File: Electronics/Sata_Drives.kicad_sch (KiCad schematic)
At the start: 66 parts, among them J20 47018-2000, J21 47018-2000, Q2 NPN, Q3 PMOS, Q4 NPN, Q5 PMOS, Q6 PMOS, Q7 NPN, Q8 NPN, Q9 PMOS, U10 JMS561, U9 W25X40CLSN, Y1 30MHz

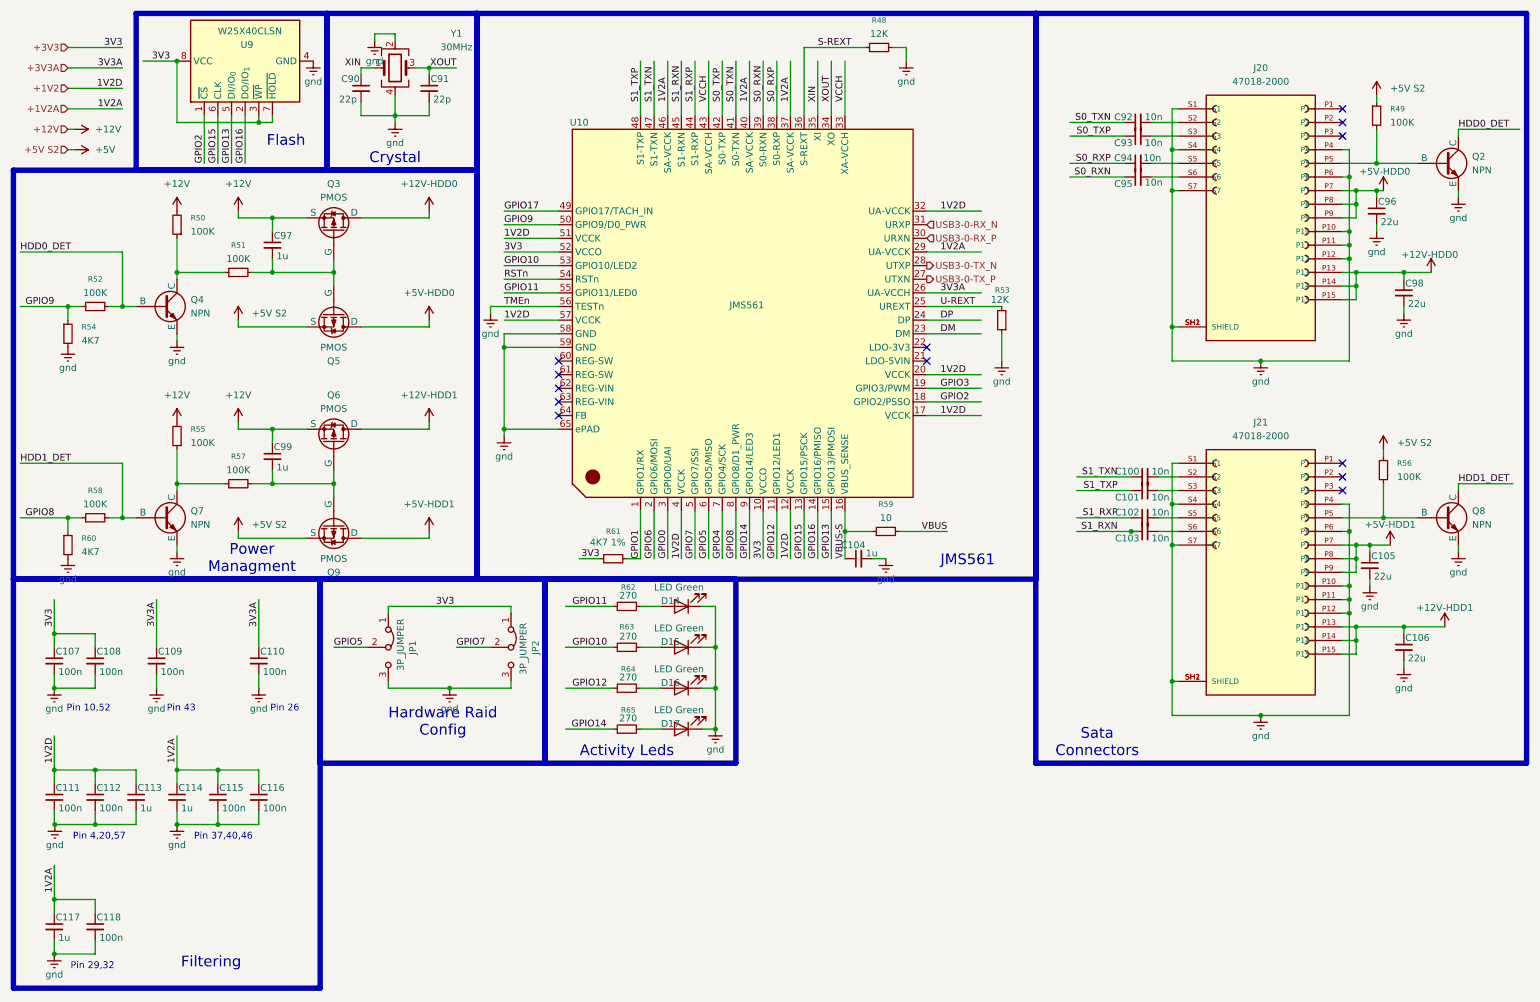
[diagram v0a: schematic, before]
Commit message: Changed sata port
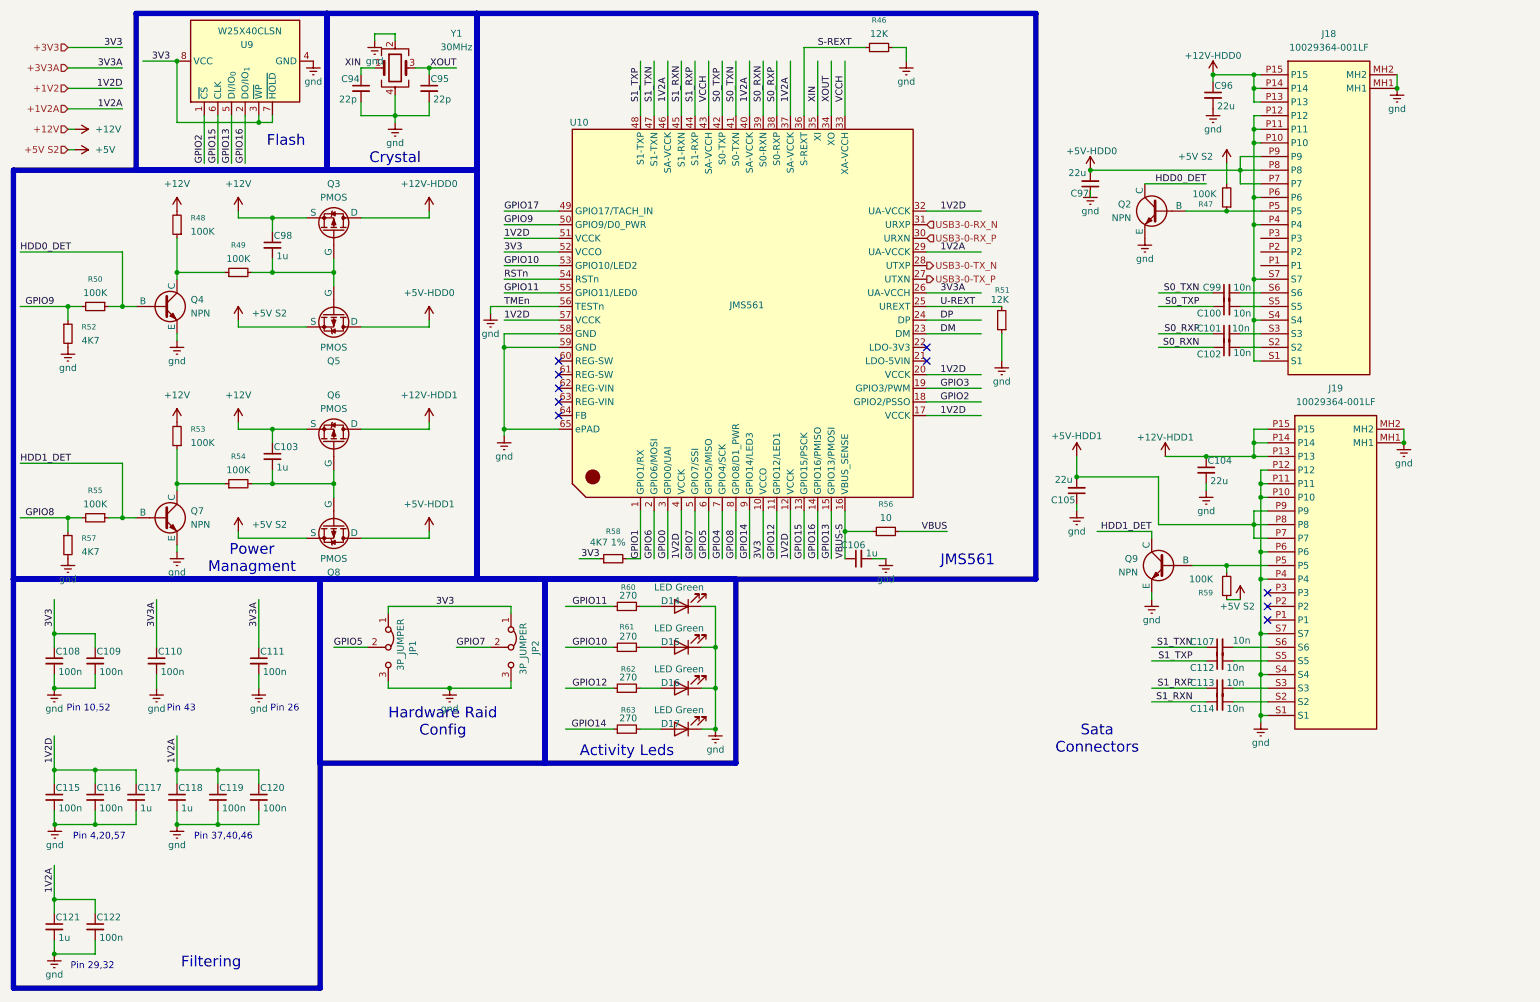
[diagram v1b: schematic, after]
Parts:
- removed C98: 22u, Capacitor_SMD:C_1206_3216Metric, symbol Device:C_Small
- removed J20, J21: 47018-2000, 47018-2000:MOLEX_47018-2000, symbol 47018-2000:47018-2000
- removed R49: 100K, Resistor_SMD:R_0603_1608Metric, symbol Device:R_Small
- added C97: 22u, Capacitor_SMD:C_1206_3216Metric, symbol Device:C_Small
- added J18, J19: 10029364-001LF, 87713-1001:87713-1001, symbol 10029364-001LF:10029364-001LF
- added R47: 100K, Resistor_SMD:R_0603_1608Metric, symbol Device:R_Small
- U10: footprint Package_DFN_QFN:QFN-64-1EP_8x8mm_P0.4mm_EP6.5x6.5mm -> Package_DFN_QFN:QFN-64-1EP_8x8mm_P0.4mm_EP6.5x6.5mm_ThermalVias
- renumbered C93 to C100, C94 to C101, C95 to C102, C99 to C103, C106 to C104, C104 to C106, C100 to C107, C107 to C108, C108 to C109, C109 to C110, C110 to C111, C101 to C112, C102 to C113, C103 to C114, C111 to C115, C112 to C116, C113 to C117, C114 to C118, C115 to C119, C116 to C120, C117 to C121, C118 to C122, C90 to C94, C91 to C95, C97 to C98, C92 to C99, Q9 to Q8, Q8 to Q9, R48 to R46, R50 to R48, R51 to R49, R52 to R50, R53 to R51, R54 to R52, R55 to R53, R57 to R54, R58 to R55, R59 to R56, R60 to R57, R61 to R58, R56 to R59, R62 to R60, R63 to R61, R64 to R62, R65 to R63
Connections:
- net +12V-HDD0: now also C96.1, J18.P13, J18.P14, J18.P15
- net +12V-HDD1: now also J19.P13, J19.P14, J19.P15
- net +5V: now also R47.2
- net +5V-HDD0: now also C97.2, J18.P7, J18.P8, J18.P9; no longer C96.1
- net +5V-HDD1: now also C105.2, J19.P7, J19.P8, J19.P9; no longer C105.1
- net gnd: now also C105.1, C97.1, J18.MH1, J18.MH2, J19.MH1, J19.MH2, J19.P10, J19.P11, J19.P12, J19.P4, J19.P6, J19.S1, J19.S4, J19.S7; no longer C105.2
- net at C113.2: now also J19.S3
- net at C107.2: now also J19.S6
- net at Q9.2 (B), R59.2: now also J19.P5
- net at C99.2: now also J18.S6
- net at C112.2: now also J19.S5
- net at C114.2: now also J19.S2
- net at Q2.2 (B): now also J18.P5, R47.1
- net at C100.2: now also J18.S5
- net at C101.2: now also J18.S3
- net at C102.2: now also J18.S2
- new net: J18.P10, J18.P11, J18.P12, J18.P4, J18.P6, J18.S1, J18.S4, J18.S7
- no-connect marks 13 -> 10
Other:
- moved on the sheet: C100, C101, C102, C104, C105, C107, C112, C113, C114, C99, Q9, R59

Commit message: More pcbing
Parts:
- removed J18, J19: 10029364-001LF, 87713-1001:87713-1001, symbol 10029364-001LF:10029364-001LF
- added J18, J19: 0877131001, 87713-1001:87713-1001, symbol 0877131001:0877131001
- renumbered C99 to C100, C100 to C101, C101 to C102, C102 to C103, C103 to C104, C104 to C105, C105 to C106, C106 to C107, C107 to C108, C108 to C109, C109 to C110, C110 to C111, C111 to C112, C112 to C113, C113 to C114, C114 to C115, C115 to C116, C116 to C117, C117 to C118, C118 to C119, C119 to C120, C120 to C121, C121 to C122, C122 to C123, C94 to C95, C95 to C96, C96 to C97, C97 to C98, C98 to C99
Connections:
- net +12V-HDD0: now also J18.20 (P13), J18.21 (P14), J18.22 (P15)
- net +12V-HDD1: now also J19.20 (P13), J19.21 (P14), J19.22 (P15)
- net +5V-HDD0: now also J18.14 (P7), J18.15 (P8), J18.16 (P9)
- net +5V-HDD1: now also J19.14 (P7), J19.15 (P8), J19.16 (P9)
- net gnd: now also J18.1 (S1), J18.11 (P4), J18.13 (P6), J18.17 (P10), J18.18 (P11), J18.19 (P12), J18.4 (S4), J18.7 (S7), J19.1 (S1), J19.11 (P4), J19.13 (P6), J19.17 (P10), J19.18 (P11), J19.19 (P12), J19.4 (S4), J19.7 (S7)
- net at C114.2: now also J19.3 (S3)
- net at C108.2: now also J19.6 (S6)
- net at Q2.2 (B), R47.1: now also J18.12 (P5)
- net at C103.2: now also J18.2 (S2)
- net at C102.2: now also J18.3 (S3)
- net at C101.2: now also J18.5 (S5)
- net at C100.2: now also J18.6 (S6)
- net at Q9.2 (B), R59.2: now also J19.12 (P5)
- net at C113.2: now also J19.5 (S5)
- net at C115.2: now also J19.2 (S2)
- no-connect marks 10 -> 13

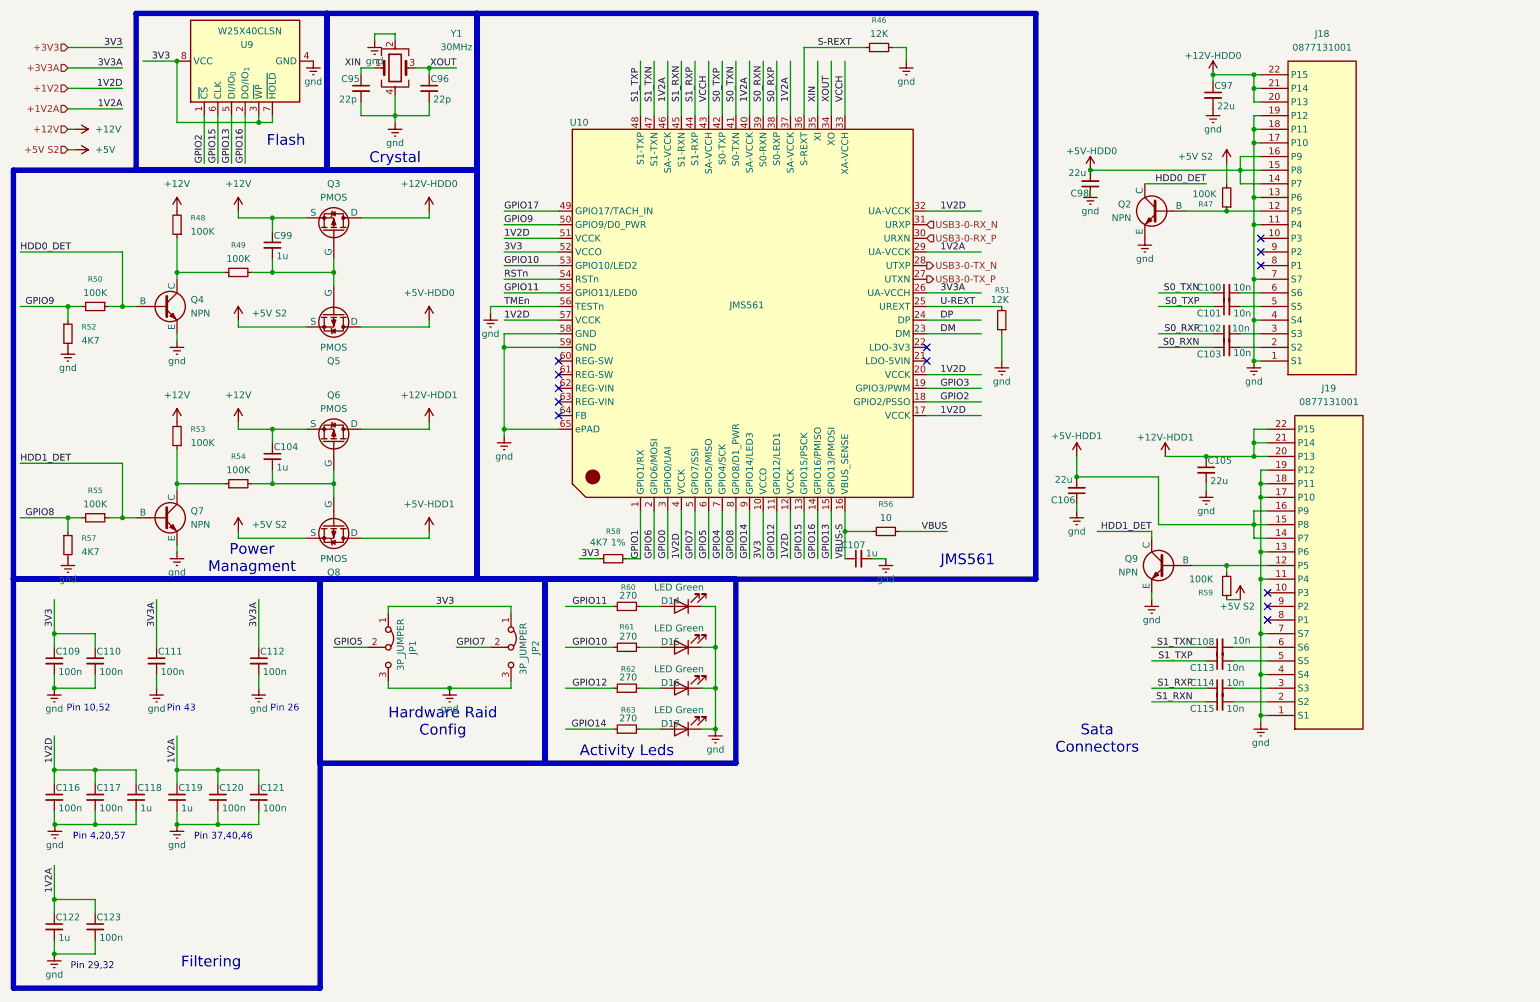
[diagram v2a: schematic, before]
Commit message: More pcb arangment, verticle ports
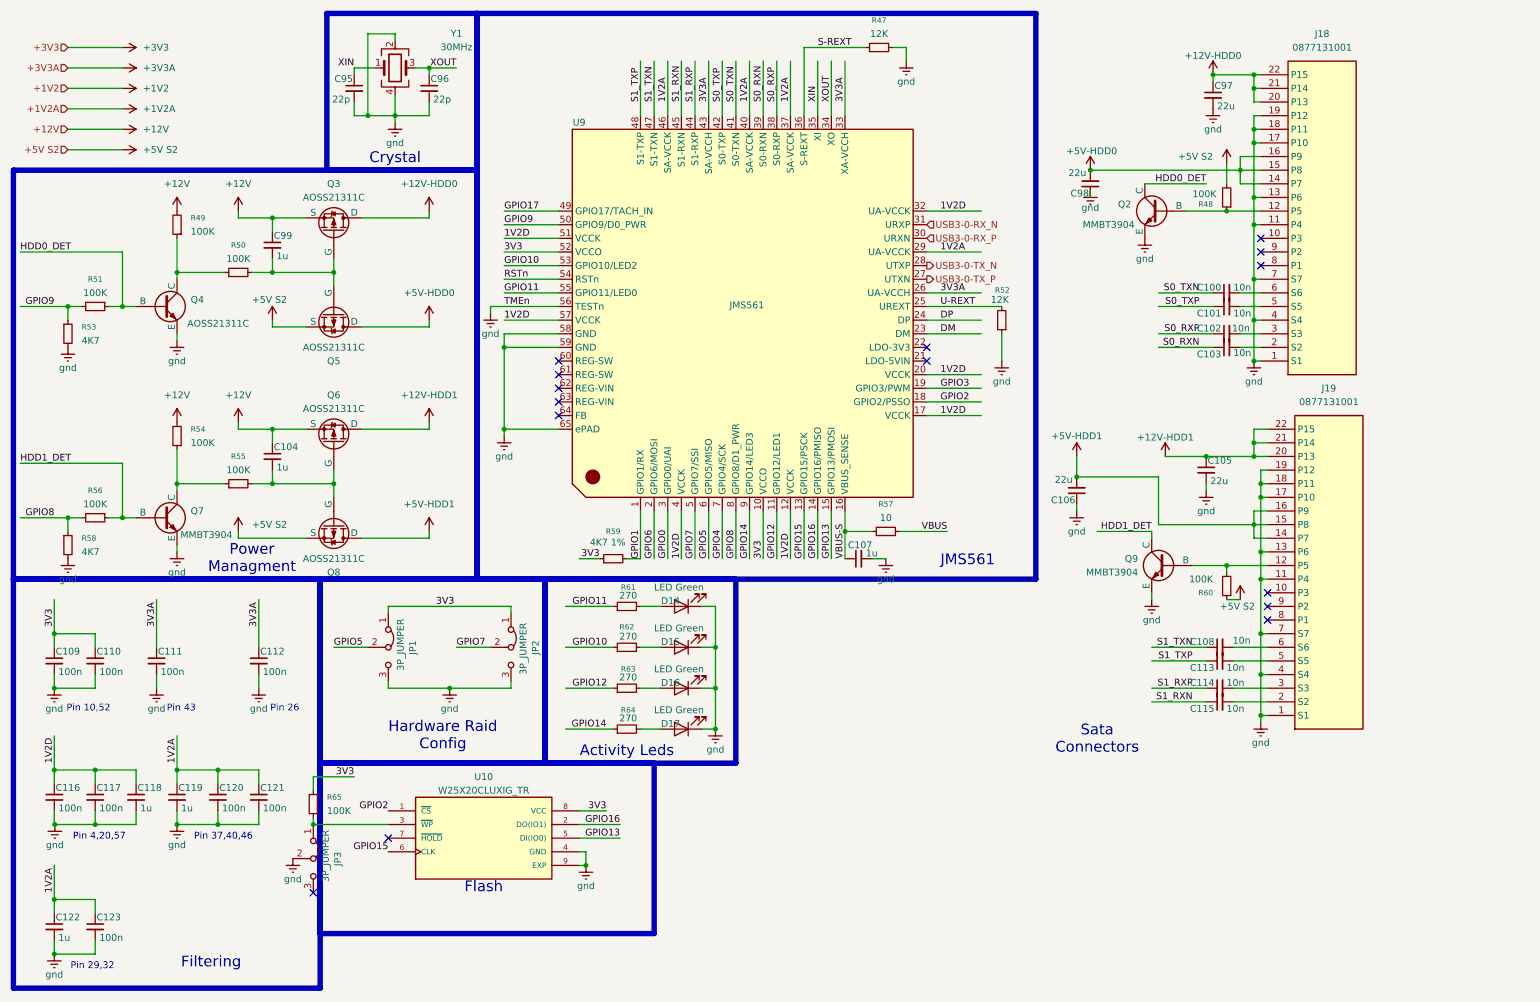
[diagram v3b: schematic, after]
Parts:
- removed U9: W25X40CLSN, Package_SO:SOIC-8_3.9x4.9mm_P1.27mm, symbol Memory_Flash:W25X40CLSN
- added JP3: 3P_JUMPER, Connector_PinHeader_2.54mm:PinHeader_1x03_P2.54mm_Vertical, symbol Jumper:Jumper_3_Bridged12
- added R65: 100K, Resistor_SMD:R_0603_1608Metric, symbol Device:R_Small
- added U10: W25X20CLUXIG_TR, W25X20CLUXIG_TR:SON50P300X200X60-9N, symbol W25X20CLUXIG_TR:W25X20CLUXIG_TR
- C109, C110, C111, C112, C116, C117, C120, C121, C123: footprint Capacitor_SMD:C_0603_1608Metric -> Capacitor_SMD:C_0402_1005Metric
- C118, C119, C122: footprint Capacitor_SMD:C_0805_2012Metric -> Capacitor_SMD:C_0402_1005Metric
- C99: footprint Capacitor_SMD:C_0805_2012Metric -> Capacitor_SMD:C_0603_1608Metric
- Q2: value NPN -> MMBT3904; footprint MMBT3904:P200_SOT-23 -> Package_TO_SOT_SMD:SOT-23
- Q3, Q5, Q6, Q8: value PMOS -> AOSS21311C; footprint AOSS21311C:SOT95P237X117-3N -> Package_TO_SOT_SMD:SOT-23-3
- Q4: value NPN -> AOSS21311C; footprint MMBT3904:P200_SOT-23 -> Package_TO_SOT_SMD:SOT-23
- Q7, Q9: value NPN -> MMBT3904
- R51: renamed from R50; footprint Resistor_SMD:R_0603_1608Metric -> Resistor_SMD:R_0402_1005Metric
- R53: renamed from R52; footprint Resistor_SMD:R_0603_1608Metric -> Resistor_SMD:R_0402_1005Metric
- renumbered R46 to R47, R47 to R48, R48 to R49, R49 to R50, R51 to R52, R53 to R54, R54 to R55, R55 to R56, R56 to R57, R57 to R58, R58 to R59, R59 to R60, R60 to R61, R61 to R62, R62 to R63, R63 to R64, U10 to U9
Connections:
- net +1V2: no longer C116.1, C117.1, C118.1, U9.12 (VCCK), U9.17 (VCCK), U9.20 (VCCK), U9.32 (UA-VCCK), U9.4 (VCCK), U9.51 (VCCK), U9.57 (VCCK)
- net +1V2A: no longer C119.1, C120.1, C121.1, C122.1, C123.1, U9.29 (UA-VCCK), U9.37 (SA-VCCK), U9.40 (SA-VCCK), U9.46 (SA-VCCK)
- net +3V3: no longer C109.1, C110.1, JP1.1 (A), JP2.1 (A), R59.1, U9.10 (VCCO), U9.52 (VCCO)
- net +3V3A: no longer C111.1, C112.1, U9.26 (UA-VCCH)
- net GPIO13: now also U10.5 (DI(IO0))
- net GPIO15: now also U10.6 (CLK)
- net GPIO16: now also U10.2 (DO(IO1))
- net GPIO2: now also U10.1 (~{CS})
- net gnd: now also JP3.2 (C), U10.4 (GND), U10.9 (EXP)
- net +5V renamed +5V S2
- net VCCH renamed 3V3A
- net 3V3A: now also C111.1, C112.1, U9.26 (UA-VCCH)
- new net: JP3.1 (A), R65.1, U10.3 (~{WP})
- new net 1V2A: C119.1, C120.1, C121.1, C122.1, C123.1, U9.29 (UA-VCCK), U9.37 (SA-VCCK), U9.40 (SA-VCCK), U9.46 (SA-VCCK)
- new net 1V2D: C116.1, C117.1, C118.1, U9.12 (VCCK), U9.17 (VCCK), U9.20 (VCCK), U9.32 (UA-VCCK), U9.4 (VCCK), U9.51 (VCCK), U9.57 (VCCK)
- new net 3V3: C109.1, C110.1, JP1.1 (A), JP2.1 (A), R59.1, R65.2, U10.8 (VCC), U9.10 (VCCO), U9.52 (VCCO)
- no-connect marks 13 -> 15
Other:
- moved on the sheet: C95

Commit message: Power symbols changed and sata hub fixed schem
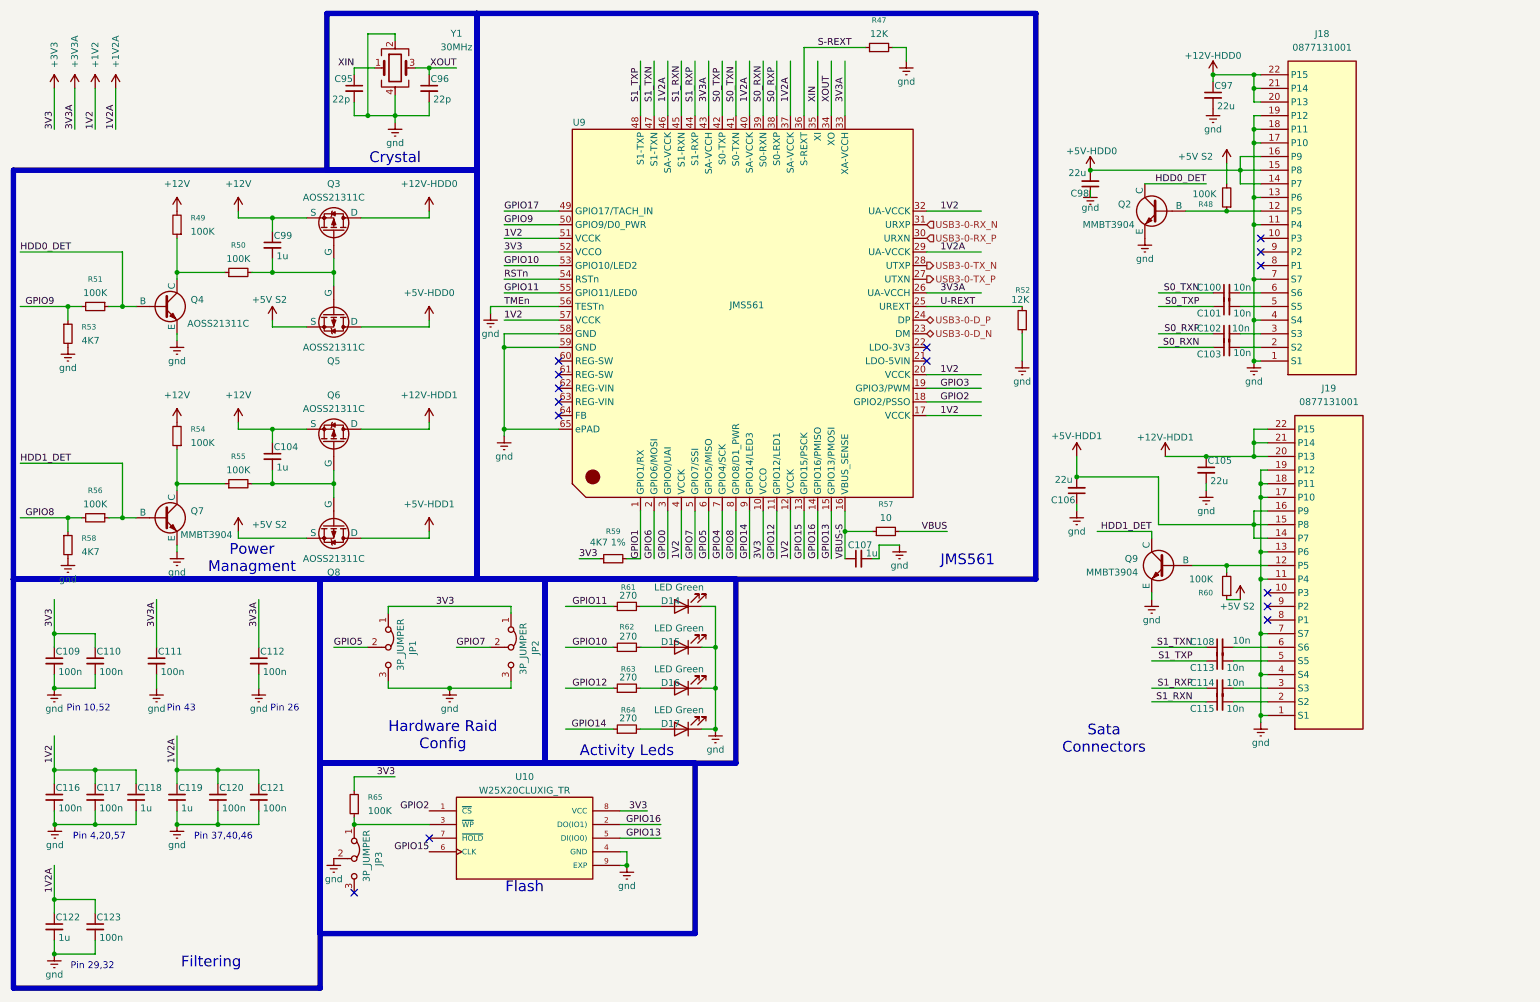
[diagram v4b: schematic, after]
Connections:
- net 1V2A is gone; now on net +1V2A: C119.1, C120.1, C121.1, C122.1, C123.1, U9.29 (UA-VCCK), U9.37 (SA-VCCK), U9.40 (SA-VCCK), U9.46 (SA-VCCK)
- net 1V2D is gone; now on net +1V2: C116.1, C117.1, C118.1, U9.12 (VCCK), U9.17 (VCCK), U9.20 (VCCK), U9.32 (UA-VCCK), U9.4 (VCCK), U9.51 (VCCK), U9.57 (VCCK)
- net 3V3 is gone; now on net +3V3: C109.1, C110.1, JP1.1 (A), JP2.1 (A), R59.1, R65.2, U10.8 (VCC), U9.10 (VCCO), U9.52 (VCCO)
- net 3V3A is gone; now on net +3V3A: C111.1, C112.1, U9.26 (UA-VCCH), U9.33 (XA-VCCH), U9.43 (SA-VCCH)
- net DM renamed USB3-0-D_N
- net DP renamed USB3-0-D_P
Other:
- moved on the sheet: JP3, R52, R65, U10
